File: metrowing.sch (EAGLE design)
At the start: 8 parts, among them SW1 SPST_TACT-KMR2, U2 ARDUINOR3-NOSILK

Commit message: correct (mkii) version
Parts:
- removed SW1: SPST_TACT-KMR2, adafruit:SPST_TACT-KMR2
- removed U$3, U$4: FIDUCIAL, adafruit:FIDUCIAL
- removed U2: ARDUINOR3-NOSILK, microbuilder:ARDUINOR3-NOSILK
- added S1: MOMENTARY-SWITCH-SPST-SMD-6.0X3.5MM, SparkFun-Switches:MOMENTARY-SWITCH-SPST-SMD-6.0X3.5MM
- added U1: ARDUINOR3-DIMENSION, 00_bsiepert:ARDUINOR3-DIMENSION
- J1: device SparkFun-Connectors:CONN_16 -> SparkFun-Connectors:CONN_12
- J2: device SparkFun-Connectors:CONN_12 -> SparkFun-Connectors:CONN_16
- MS1, MS2: value FEATHERWING_NODIM -> FEATHERWING_PINS; device microbuilder:FEATHERWING_NODIM -> 00_bsiepert:FEATHERWING_PINS
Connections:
- removed net 3V: J1.2, MS1.3V, MS2.3V, U2.3V
- removed net N$5: J2.2, MS1.EN, MS2.EN
- removed net RST: J1.1, MS1.!RESET, MS2.!RESET
- new net 3V3: J2.2, MS1.3V3, MS2.3V3, U1.3V
- new net D2: U1.D2
- new net D3: U1.D3
- new net D4: U1.D4
- new net D7: U1.D7
- new net D8: U1.D8
- new net ENABLE: J1.11, MS1.EN, MS2.EN
- new net IOREF: U1.IOREF
- new net N$153: U1.VIN
- new net N$4: U1.RESERVED
- net +5V: now also U1.5V; no longer U2.5V
- net A0: now also J2.5, MS1.A0, MS2.A0, U1.A0; no longer J1.5, MS1.GPIOA0, MS2.GPIOA0, U2.A0
- net A1: now also J2.6, MS1.A1, MS2.A1, U1.A1; no longer J1.6, MS1.GPIOA1, MS2.GPIOA1, U2.A1
- net A2: now also J2.7, MS1.A2, MS2.A2, U1.A2; no longer J1.7, MS1.GPIOA2, MS2.GPIOA2, U2.A2
- net A3: now also J2.8, MS1.A3, MS2.A3, U1.A3; no longer J1.8, MS1.GPIOA3, MS2.GPIOA3, U2.A3
- net A4: now also J2.9, MS1.A4, MS2.A4, U1.A4/SDA; no longer J1.9, MS1.GPIOA4, MS2.GPIOA4, U2.A4/SDA
- net A5: now also J2.10, MS1.A5, MS2.A5, U1.A5/SCL; no longer J1.10, MS1.GPIOA5, MS2.GPIOA5, U2.A5/SCL
- net AREF: now also J2.3, U1.AREF; no longer J1.3, U2.AREF
- net D0: now also J2.14, MS1.D0_RX, MS2.D0_RX, U1.D0; no longer J1.14, MS1.GPIORX, MS2.GPIORX, U2.D0
- net D1: now also J2.15, MS1.D1_TX, MS2.D1_TX, U1.D1; no longer J1.15, MS1.GPIOTX, MS2.GPIOTX, U2.D1
- net D10: now also J1.6, MS1.D10, MS2.D10, U1.D10; no longer J2.7, MS1.GPIO10, MS2.GPIO10
- net D11: now also J1.7, MS1.D11, MS2.D11, U1.D11; no longer J2.6, MS1.GPIO11, MS2.GPIO11
- net D12: now also J1.8, MS1.D12, MS2.D12, U1.D12; no longer J2.5, MS1.GPIO12, MS2.GPIO12
- net D13: now also J1.9, MS1.D13, MS2.D13, U1.D13; no longer J2.4, MS1.GPIO13, MS2.GPIO13
- net D5: now also J1.3, MS1.D5, MS2.D5, U1.D5; no longer J2.10, MS1.GPIO5, MS2.GPIO5
- net D6: now also J1.4, MS1.D6, MS2.D6, U1.D6; no longer J2.9, MS1.GPIO6, MS2.GPIO6
- net D9: now also J1.5, MS1.D9, MS2.D9, U1.D9; no longer J2.8, MS1.GPIO9, MS2.GPIO9
- net GND: now also J2.16, J2.4, MS1.GND2, MS2.GND2, S1.1, U1.GND, U1.GND1, U1.GND2; no longer J1.16, J1.4, MS1.NC, MS2.NC, SW1.P, SW1.P1, U2.GND, U2.GND1, U2.GND2
- net MISO: now also J2.13, MS1.MISO, MS2.MISO; no longer J1.13, MS1.GPIOMISO, MS2.GPIOMISO
- net MOSI: now also J2.12, MS1.MOSI, MS2.MOSI; no longer J1.12, MS1.GPIOMOSI, MS2.GPIOMOSI
- net RESET: now also J2.1, MS1.RST, MS2.RST, S1.2, U1./RESET; no longer SW1.S, SW1.S1, U2./RESET
- net SCK: now also J2.11, MS1.SCK, MS2.SCK; no longer J1.11, MS1.GPIOSCK, MS2.GPIOSCK
- net SCL: now also J1.2, MS1.SCL, MS2.SCL, U1.SCL; no longer J2.11, MS1.GPIOSCL, MS2.GPIOSCL, U2.SCL
- net SDA: now also J1.1, MS1.SDA, MS2.SDA, U1.SDA; no longer J2.12, MS1.GPIOSDA, MS2.GPIOSDA, U2.SDA
- net USB: now also J1.10; no longer J2.3
- net VBAT: now also J1.12; no longer J2.1

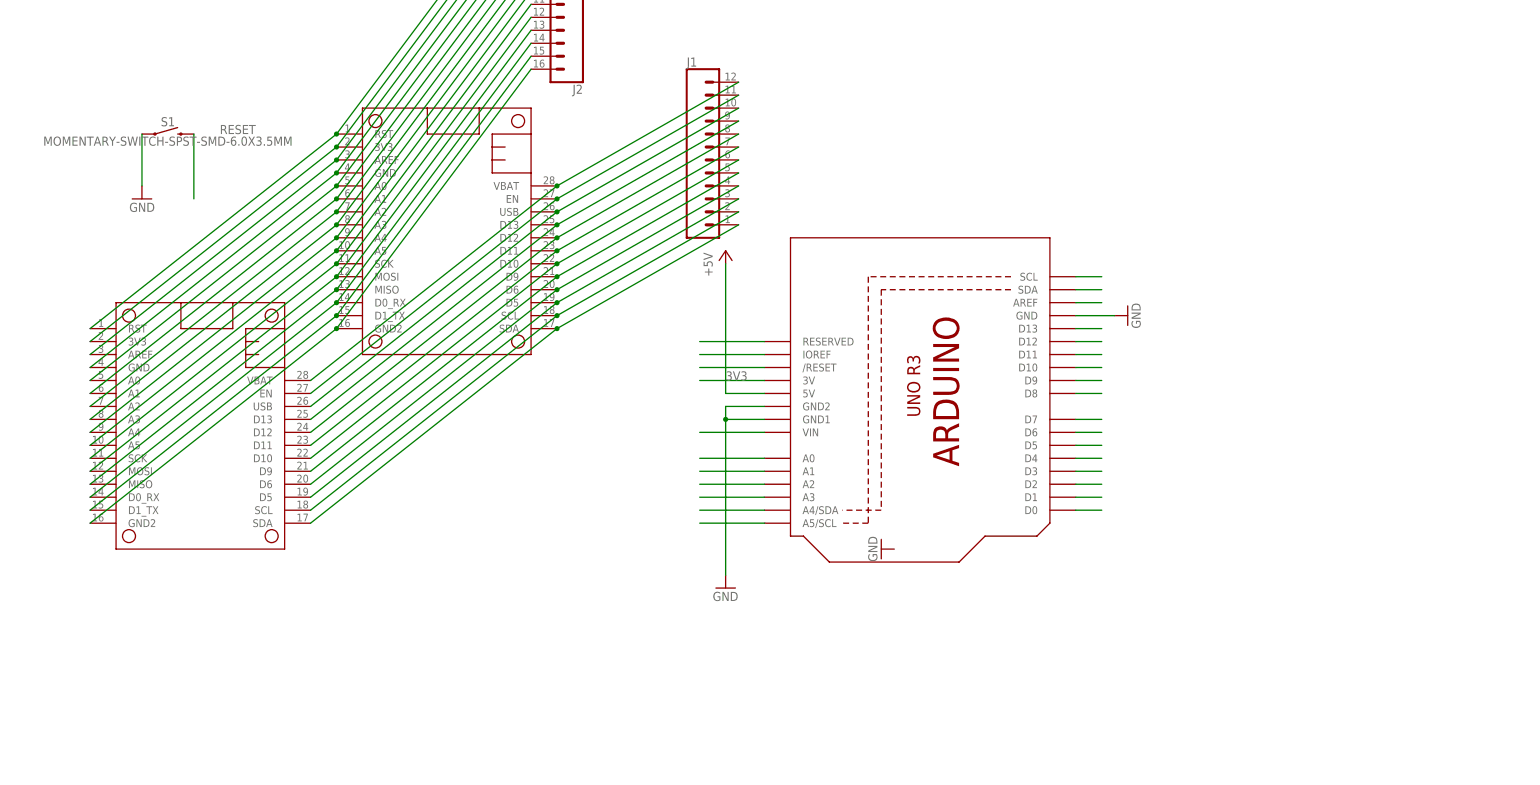
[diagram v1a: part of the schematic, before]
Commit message: updated and fixed mkii: Now with more SPI
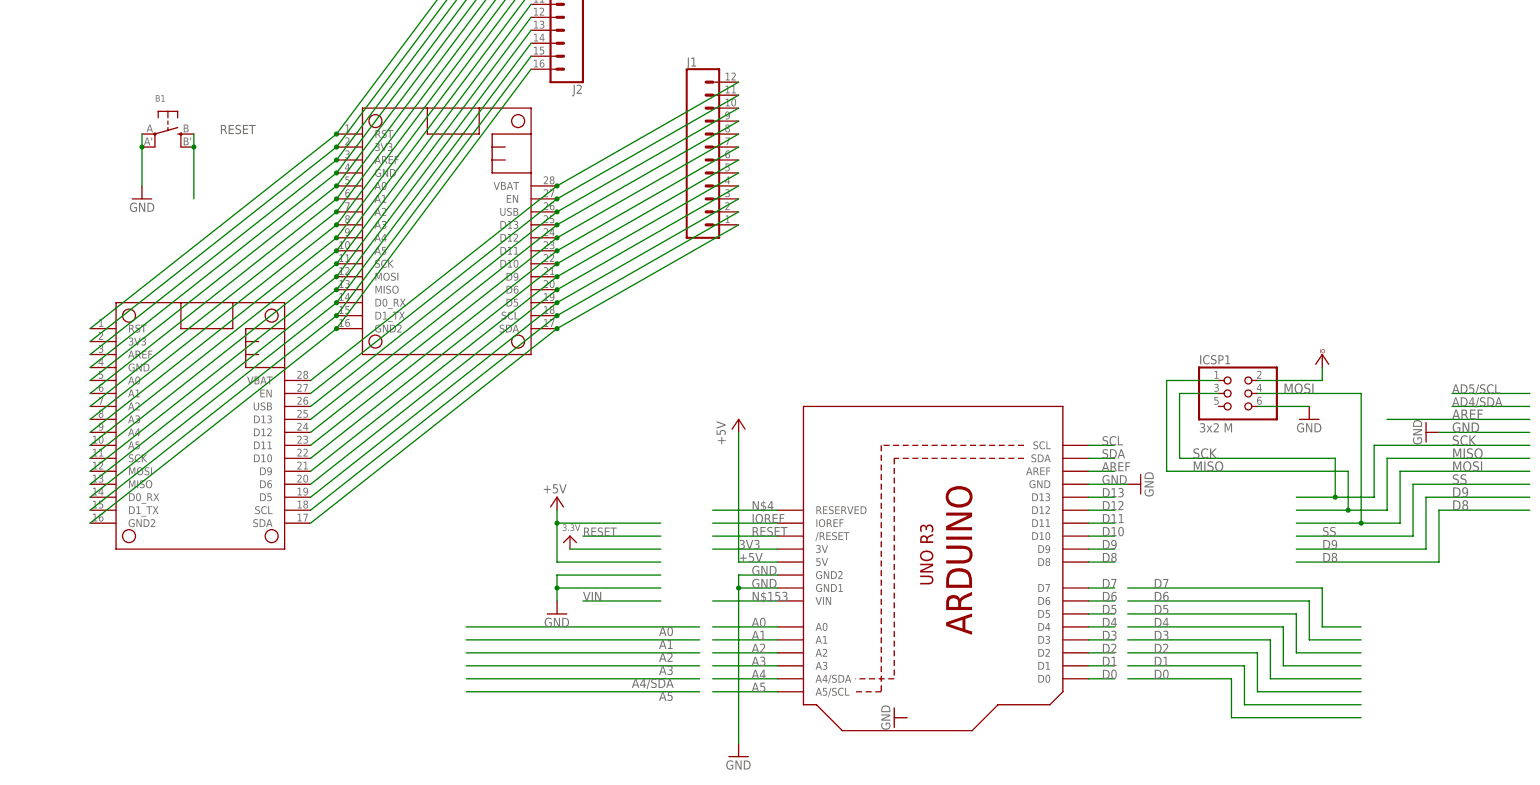
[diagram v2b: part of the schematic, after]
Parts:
- removed S1: MOMENTARY-SWITCH-SPST-SMD-6.0X3.5MM, SparkFun-Switches:MOMENTARY-SWITCH-SPST-SMD-6.0X3.5MM
- added B1: (no value), microbuilder:SWITCH_TACT_SMT
- added ICSP1: 3x2 M, microbuilder:HEADER-2X3
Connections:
- removed net USB: J1.10, MS1.USB, MS2.USB
- new net VCCIO: ICSP1.2
- net +5V: now also J1.10, MS1.USB, MS2.USB
- net GND: now also B1.P, B1.P1, ICSP1.6; no longer S1.1
- net MISO: now also ICSP1.1
- net MOSI: now also ICSP1.4
- net RESET: now also B1.S, B1.S1; no longer S1.2
- net SCK: now also ICSP1.3
